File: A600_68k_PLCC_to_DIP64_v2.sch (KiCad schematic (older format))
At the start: 6 parts, among them U1 MC68000_PLCC68, U2 68000_SOCKET

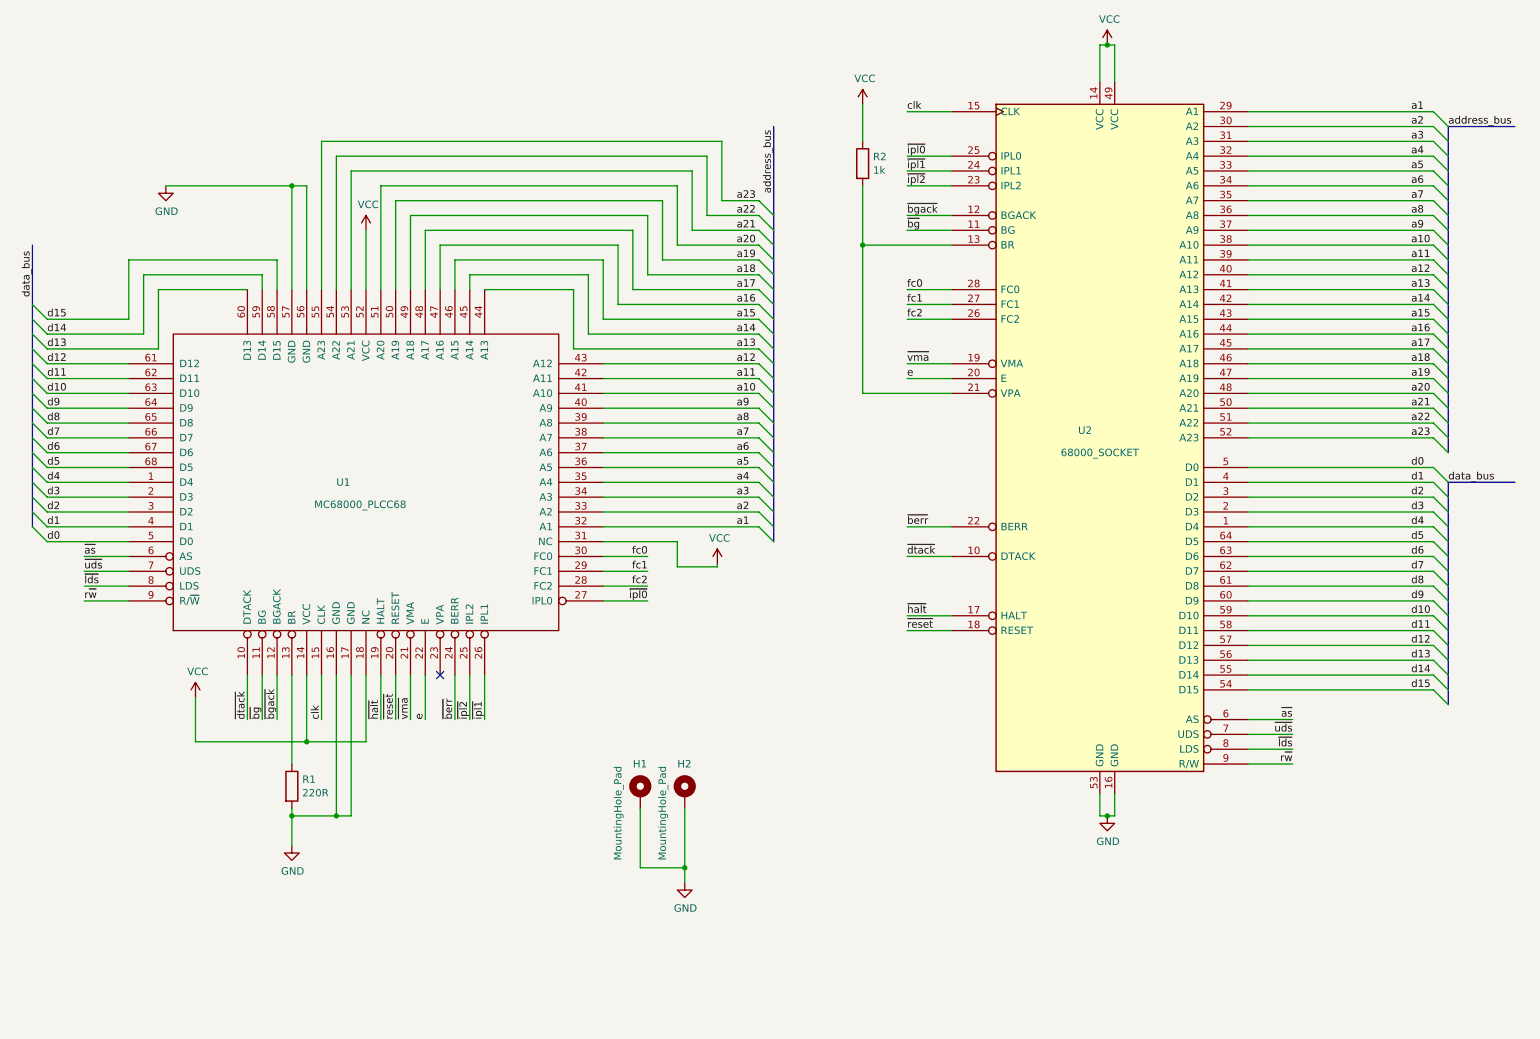
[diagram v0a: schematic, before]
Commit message: Updated to Rev B
Re-routed 4-layer design.
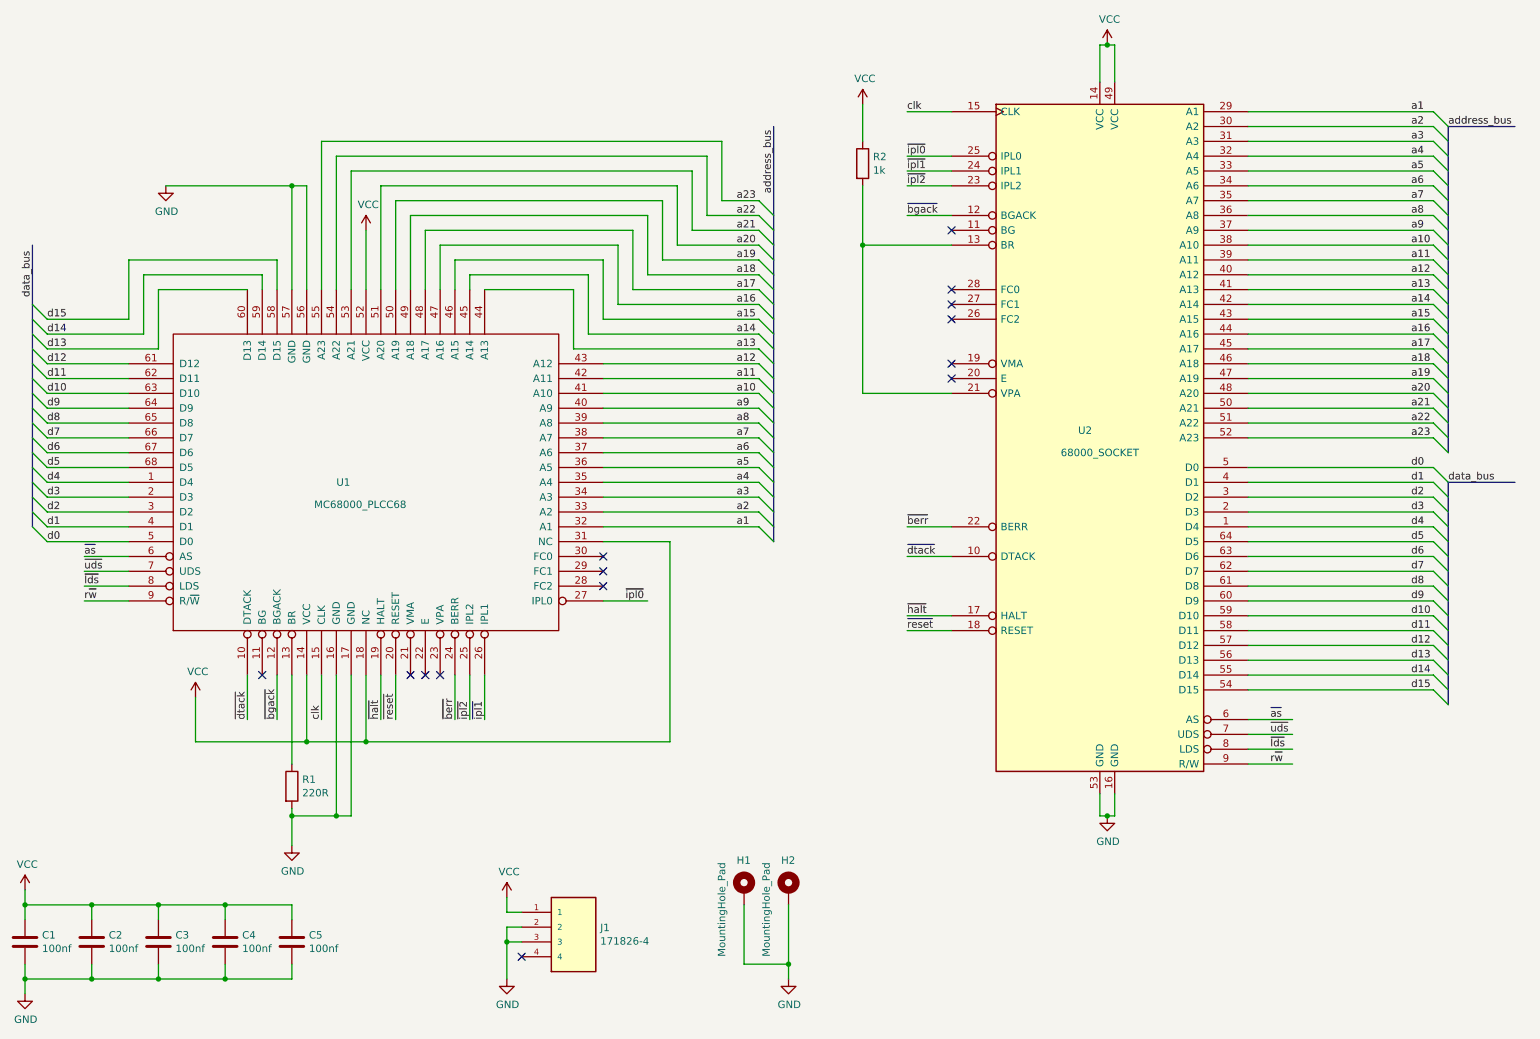
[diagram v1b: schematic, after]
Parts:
- added C1, C2, C3, C4, C5: 100nf, Capacitor_SMD:C_0805_2012Metric_Pad1.18x1.45mm_HandSolder, symbol Device:C
- added J1: 171826-4, A600 68k PLCC to DIP64 v2:TE_171826-4, symbol 171826-4:171826-4
- R1, R2: footprint Resistor_SMD:R_0805_2012Metric_Pad1.15x1.40mm_HandSolder -> Resistor_SMD:R_0805_2012Metric_Pad1.20x1.40mm_HandSolder
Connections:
- net GND: now also C1.2, C2.2, C3.2, C4.2, C5.2, J1.2, J1.3
- net VCC: now also C1.1, C2.1, C3.1, C4.1, C5.1, J1.1
- net e: no longer names the net of U1.22 (E)
- net e: no longer U2.20 (E)
- net fc0: no longer names the net of U1.30 (FC0)
- net fc0: no longer U2.28 (FC0)
- net fc1: no longer names the net of U1.29 (FC1)
- net fc1: no longer U2.27 (FC1)
- net fc2: no longer names the net of U1.28 (FC2)
- net fc2: no longer U2.26 (FC2)
- net ~bg: no longer names the net of U1.11 (BG)
- net ~bg: no longer U2.11 (BG)
- net ~vma: no longer names the net of U1.21 (VMA)
- net ~vma: no longer U2.19 (VMA)
- no-connect marks 1 -> 14
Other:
- moved on the sheet: H1, H2

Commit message: Added GND vias, and corrected cap values
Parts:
- C1, C2, C3, C4, C5: value 100nf -> 10uf
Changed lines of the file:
@@
 P 850 7000
 F 0 "C1" H 965 7046 50  0000 L CNN
-F 1 "100nf" H 965 6955 50  0000 L CNN
+F 1 "10uf" H 965 6955 50  0000 L CNN
 F 2 "Capacitor_SMD:C_0805_2012Metric_Pad1.18x1.45mm_HandSolder" H 888 6850 50  0001 C CNN
 F 3 "~" H 850 7000 50  0001 C CNN
@@
 P 1300 7000
 F 0 "C2" H 1415 7046 50  0000 L CNN
-F 1 "100nf" H 1415 6955 50  0000 L CNN
+F 1 "10uf" H 1415 6955 50  0000 L CNN
 F 2 "Capacitor_SMD:C_0805_2012Metric_Pad1.18x1.45mm_HandSolder" H 1338 6850 50  0001 C CNN
 F 3 "~" H 1300 7000 50  0001 C CNN
@@
 P 1750 7000
 F 0 "C3" H 1865 7046 50  0000 L CNN
-F 1 "100nf" H 1865 6955 50  0000 L CNN
+F 1 "10uf" H 1865 6955 50  0000 L CNN
 F 2 "Capacitor_SMD:C_0805_2012Metric_Pad1.18x1.45mm_HandSolder" H 1788 6850 50  0001 C CNN
 F 3 "~" H 1750 7000 50  0001 C CNN
@@
 P 2200 7000
 F 0 "C4" H 2315 7046 50  0000 L CNN
-F 1 "100nf" H 2315 6955 50  0000 L CNN
+F 1 "10uf" H 2315 6955 50  0000 L CNN
 F 2 "Capacitor_SMD:C_0805_2012Metric_Pad1.18x1.45mm_HandSolder" H 2238 6850 50  0001 C CNN
 F 3 "~" H 2200 7000 50  0001 C CNN
@@
 P 2650 7000
 F 0 "C5" H 2765 7046 50  0000 L CNN
-F 1 "100nf" H 2765 6955 50  0000 L CNN
+F 1 "10uf" H 2765 6955 50  0000 L CNN
 F 2 "Capacitor_SMD:C_0805_2012Metric_Pad1.18x1.45mm_HandSolder" H 2688 6850 50  0001 C CNN
 F 3 "~" H 2650 7000 50  0001 C CNN
